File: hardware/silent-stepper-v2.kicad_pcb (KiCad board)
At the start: 4 copper layers, 80 x 80 mm, 89 parts, among them P1 VIN, P101 CON-SENSOR2, P102 DEBUG, P103 BOOT, P2 OUT, P3 GPIO, P4 PROTO, Q1 CSD19533Q5A, Q2 CSD19533Q5A, Q3 CSD19533Q5A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

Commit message: finished prototype ready for revision
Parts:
- removed R101: 1k, kicad-libraries:R0603F
- added C30: 100nF, kicad-libraries:C0603F, F.Cu at (58.5, 98.8)
- added D3: red, kicad-libraries:D0603E, F.Cu at (98.7, 93.0)
- added D4: blue, kicad-libraries:D0603E, F.Cu at (112.8, 93.0)
- added D5: blue, kicad-libraries:D0603E, F.Cu at (117.5, 93.0)
- added D6: blue, kicad-libraries:D0603E, F.Cu at (108.1, 93.0)
- added D7: blue, kicad-libraries:D0603E, F.Cu at (103.4, 93.0)
- added G***: LOGO, kicad-libraries:Logo_CoMCU, B.Cu at (85.0, 101.9)
- added G***: LOGO, kicad-libraries:Logo_TF_10x12, F.Cu at (51.0, 104.8)
- added R25: 1k, kicad-libraries:R0603F, F.Cu at (108.4, 98.5)
- added R26: 1k, kicad-libraries:R0603F, F.Cu at (103.2, 98.5)
- added RP4: 1k, kicad-libraries:0603X4, F.Cu at (105.8, 98.5)
- added U4: DRILL, kicad-libraries:DRILL_NP, F.Cu at (47.5, 142.5)
- added U5: DRILL, kicad-libraries:DRILL_NP, F.Cu at (47.5, 117.5)
- added U6: DRILL, kicad-libraries:DRILL_NP, F.Cu at (122.5, 117.5)
- added U7: DRILL, kicad-libraries:DRILL_NP, F.Cu at (122.5, 142.5)
- added VAL: CE_5mm, kicad-libraries:CE_5mm, B.Cu at (93.0, 101.9)
- added VAL: WEEE_7mm, kicad-libraries:WEEE_7mm, B.Cu at (77.8, 102.4)
- C3: value 100nF -> 220nF
- RP2: footprint kicad-libraries:0603X4 -> kicad-libraries:4X0402
- moved D101 71.1 mm to (94.0, 93.0), turned to 270 degrees
- moved C102 63.5 mm to (88.6, 97.4), turned to 90 degrees
- moved RP101 60.2 mm to (86.9, 97.4)
- moved C2 46.5 mm to (69.3, 103.1), turned to 270 degrees
- moved X1 43.8 mm to (71.7, 99.7), turned to 90 degrees
- moved C1 42.4 mm to (71.7, 102.0), turned to 180 degrees
- moved C4 39.6 mm to (71.7, 97.4)
- moved P102 38.1 mm to (65.3, 92.0)
- moved P103 34.5 mm to (63.5, 91.9), turned to 270 degrees
- moved C104 33.7 mm to (61.5, 104.2), turned to 180 degrees
- moved RP1 30.8 mm to (64.7, 110.2), turned to 180 degrees
- moved C3 21.3 mm to (57.0, 98.8), turned to 90 degrees
- moved P4 20.1 mm to (123.6, 102.2), turned to 90 degrees
- moved R23 15.2 mm to (53.9, 149.9)
- moved P3 15.2 mm to (47.8, 155.2)
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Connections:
- RP1 pad 5: DIAG1 -> Net-(RP1-Pad5)
- RP1 pad 6: DIAG0 -> Net-(RP1-Pad6)
- RP1 pad 8: DRV_ENN -> Net-(RP1-Pad8)
- RP101 pad 1: Net-(P101-Pad4) -> S-CS
- RP101 pad 2: Net-(P101-Pad5) -> S-CLK
- RP101 pad 3: Net-(P101-Pad6) -> S-MOSI
- RP101 pad 4: Net-(C102-Pad2) -> S-MISO
- RP101 pad 5: S-MISO -> Net-(C102-Pad2)
- RP101 pad 6: S-MOSI -> Net-(P101-Pad6)
- RP101 pad 7: S-CLK -> Net-(P101-Pad5)
- RP101 pad 8: S-CS -> Net-(P101-Pad4)
- RP3 pad 5: Net-(RP3-Pad5) -> Net-(RP1-Pad8)
- RP3 pad 7: Net-(RP3-Pad7) -> Net-(RP1-Pad6)
- RP3 pad 8: Net-(RP3-Pad8) -> Net-(RP1-Pad5)
- U1 pad 23: Net-(P4-Pad2) -> Net-(P4-Pad3)
- U1 pad 24: Net-(P4-Pad3) -> Net-(P4-Pad2)
- U1 pad 26: Net-(RP3-Pad7) -> Net-(RP1-Pad6)
- U1 pad 27: Net-(RP3-Pad8) -> Net-(RP1-Pad5)
- U1 pad 28: Net-(RP3-Pad5) -> Net-(RP1-Pad8)
- U2 pad 11: Net-(U2-Pad11) -> GPIO0
- U2 pad 12: Net-(U2-Pad12) -> GPIO1
- U2 pad 13: Net-(P102-Pad1) -> Net-(U2-Pad13)
- U2 pad 4: GPIO0 -> Net-(P102-Pad1)
- U2 pad 5: GPIO1 -> Net-(U2-Pad5)
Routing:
- net VCC: track 0.00 -> 151.2 mm, vias 0 -> 4
- net Net-(R25-Pad2): track 0.00 -> 60.2 mm, vias 0 -> 2
- net Net-(RP4-Pad8): track 0.00 -> 58.7 mm, vias 0 -> 2
- net GND: track 8.45 -> 66.4 mm, vias 52 -> 142
- net Net-(RP4-Pad7): track 0.00 -> 56.1 mm, vias 0 -> 2
- net Net-(RP4-Pad6): track 0.00 -> 55.2 mm, vias 0 -> 2
- net Net-(RP4-Pad5): track 0.00 -> 54.9 mm, vias 0 -> 2
- net Net-(R26-Pad2): track 0.00 -> 49.8 mm, vias 0 -> 2
- net GPIO0: track 0.00 -> 41.8 mm
- net GPIO1: track 0.00 -> 41.6 mm
- net Net-(P4-Pad1): track 0.00 -> 39.0 mm, vias 0 -> 1
- net Net-(P4-Pad2): track 0.00 -> 37.1 mm, vias 0 -> 1
- net Net-(P4-Pad3): track 0.00 -> 36.0 mm, vias 0 -> 1
- net Net-(P4-Pad4): track 0.00 -> 33.5 mm, vias 0 -> 1
- net Net-(P4-Pad5): track 0.00 -> 33.5 mm, vias 0 -> 1
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- added copper zone on In2.Cu, net GND
- added copper zone on In1.Cu, net Net-(C13-Pad1)
- added copper zone on In2.Cu, net Net-(C13-Pad1)
- added copper zone on In1.Cu, net Net-(C14-Pad1)
- added copper zone on In2.Cu, net Net-(C14-Pad1)
- added copper zone on In1.Cu, net Net-(C15-Pad1)
- added copper zone on In2.Cu, net Net-(C15-Pad1)
- added copper zone on In1.Cu, net Net-(C16-Pad1)
- added copper zone on In2.Cu, net Net-(C16-Pad1)
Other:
- rule pad_to_mask_clearance: 0.051 -> 0
- board text added: "+"
- board text added: "-"
- board text added: "ENCA"
- board text added: "ENCB"
- board text added: "ENCN"
- board text added: "Enable"
- board text added: "Error"
- board text added: "GPIO0"
- board text added: "GPIO1"
- board text added: "Input 10-48V"
- board text added: "MA1"
- board text added: "MA2"
- board text added: "MB1"
- board text added: "MB2"
- board text added: "REFL"
- board text added: "REFR"
- board text added: "Silent Stepper 2.0"
- board text added: "Status"
- board text added: "Steps"

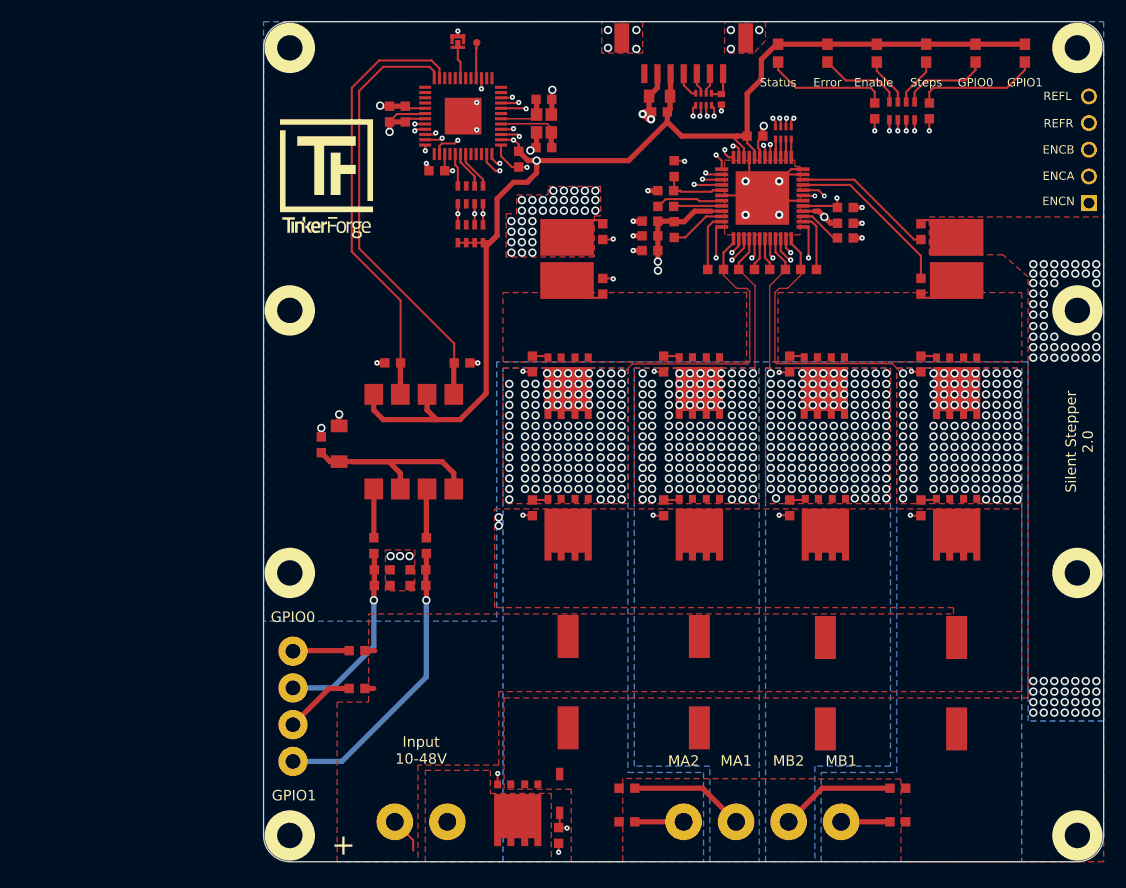
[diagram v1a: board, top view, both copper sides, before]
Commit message: changes protection circuit
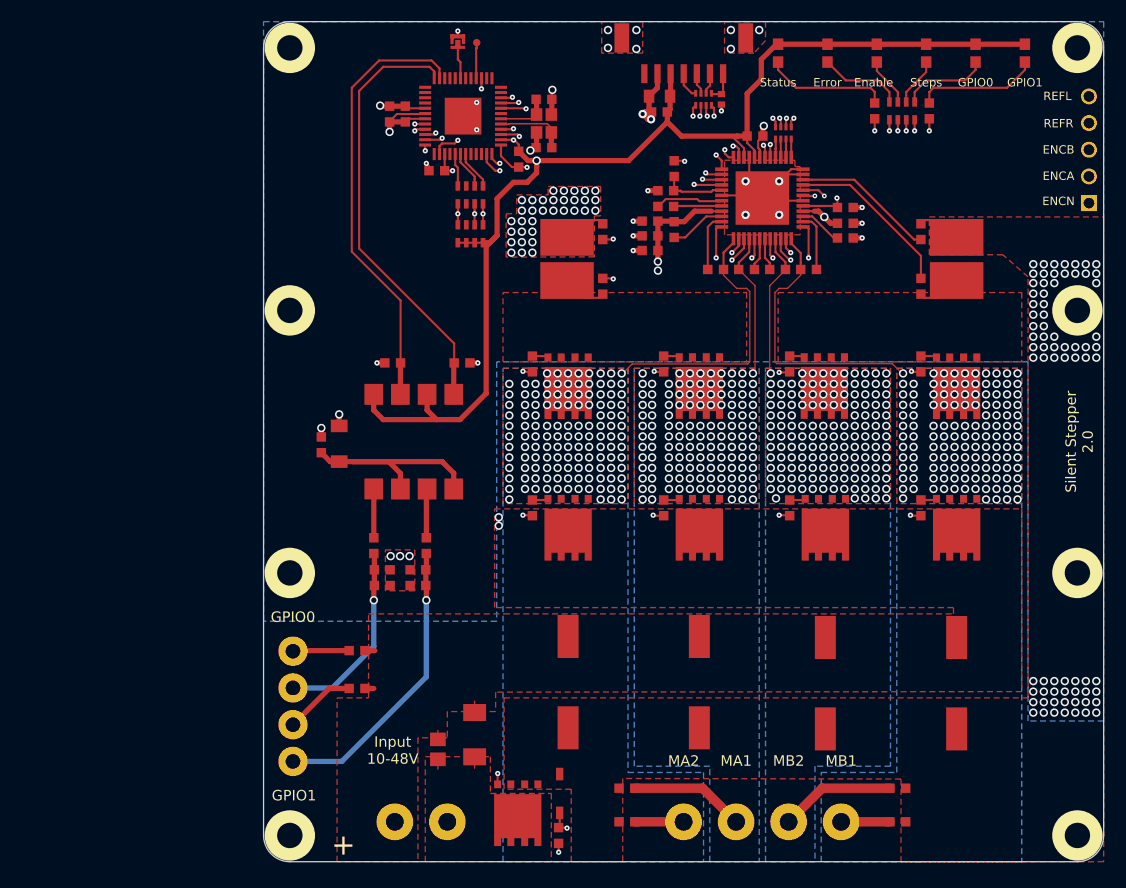
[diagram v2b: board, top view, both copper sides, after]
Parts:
- removed G***: LOGO, kicad-libraries:Logo_CoMCU
- removed G***: LOGO, kicad-libraries:Logo_TF_10x12
- removed VAL: CE_5mm, kicad-libraries:CE_5mm
- removed VAL: WEEE_7mm, kicad-libraries:WEEE_7mm
- added D8: SMBJ24CA, kicad-libraries:SMB, F.Cu at (65.1, 157.9)
- added PTC1: VC080526C580DP, kicad-libraries:R0805E, F.Cu at (61.6, 159.3)
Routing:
- net Net-(D8-Pad2): track 0.00 -> 2.04 mm
- net V_GPIO: track 91.9 -> 90.4 mm
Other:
- board text added: "IN"

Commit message: ready for prototype
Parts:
- added Fiducial_Mark: VAL**, kicad-libraries:Fiducial_Mark, F.Cu at (101.0, 114.0)
- added Fiducial_Mark: VAL**, kicad-libraries:Fiducial_Mark, F.Cu at (64.0, 143.0)
- added Fiducial_Mark: VAL**, kicad-libraries:Fiducial_Mark, F.Cu at (116.0, 99.0)
- added Fiducial_Mark: VAL**, kicad-libraries:Fiducial_Mark, F.Cu at (53.0, 94.0)
- added G***: LOGO, kicad-libraries:TF_LOGO_70MM, B.Cu at (85.0, 103.5)
- added G***: LOGO, kicad-libraries:Logo_CoMCU, B.Cu at (85.0, 153.0)
- added G***: LOGO, kicad-libraries:Logo_TF_10x12, F.Cu at (52.0, 108.5)
- added VAL: WEEE_7mm, kicad-libraries:WEEE_7mm, B.Cu at (76.9, 153.4)
- added VAL: CE_5mm, kicad-libraries:CE_5mm, B.Cu at (93.0, 153.0)

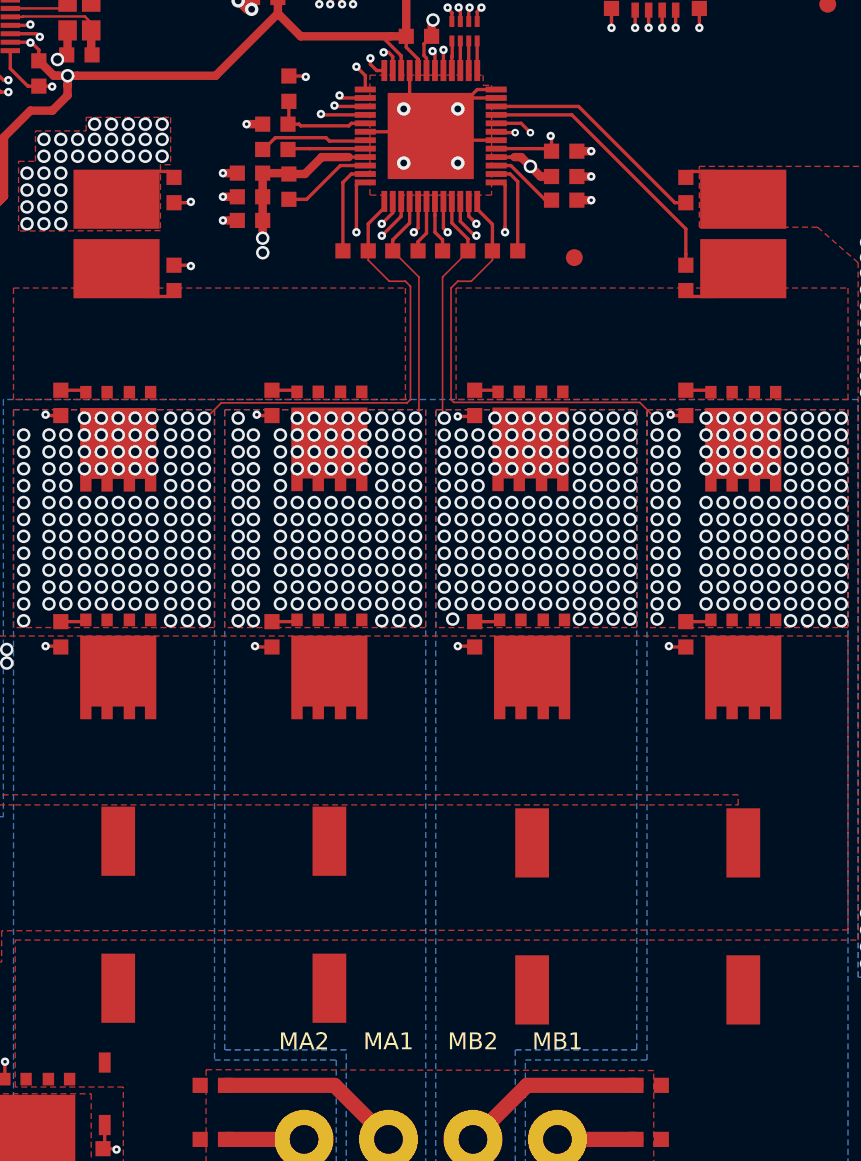
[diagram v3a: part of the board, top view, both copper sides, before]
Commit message: DRC control and ordered prototyp
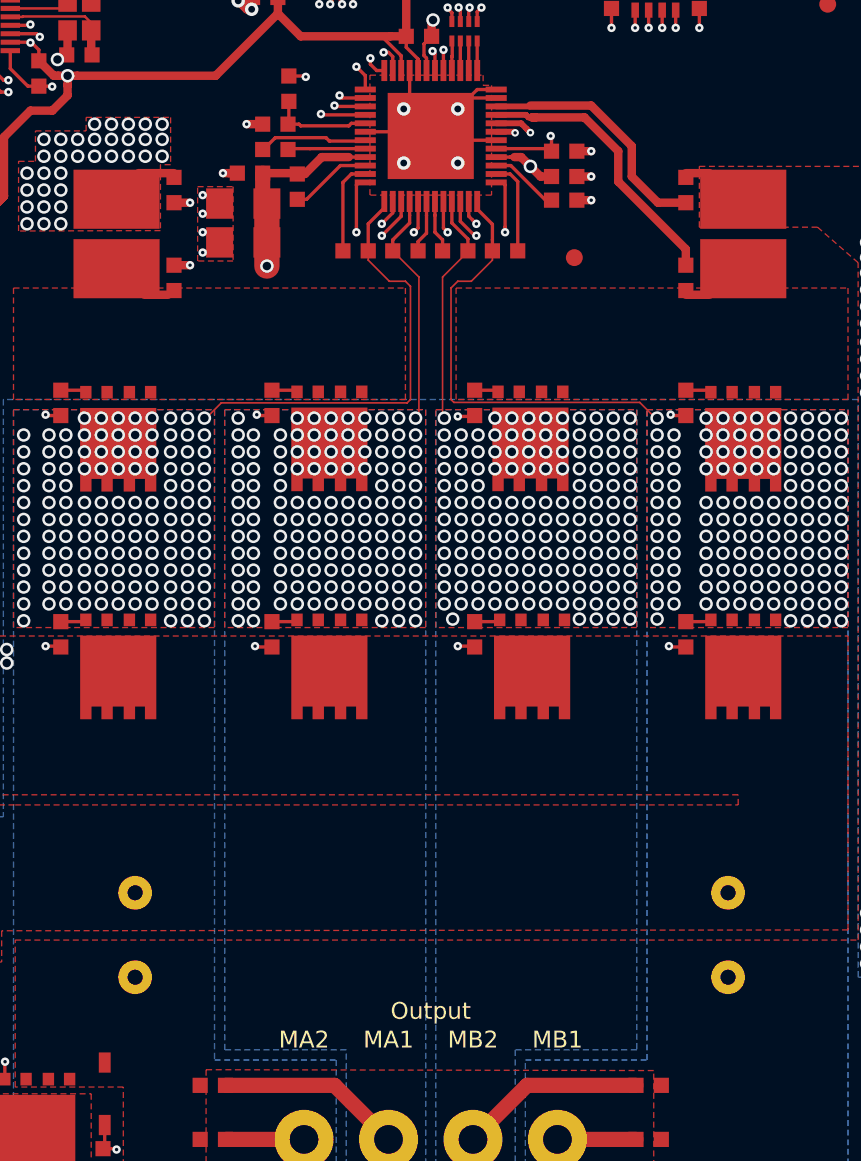
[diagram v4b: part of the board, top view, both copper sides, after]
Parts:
- removed C19, C22: 220uF/100V/LowESR, kicad-libraries:ELKO_103
- C17, C18: footprint kicad-libraries:C0603F -> kicad-libraries:C1206E
- C20, C21: value 220uF/100V/LowESR -> 220uF/100V/UVY2A221MHD1TO; footprint kicad-libraries:ELKO_103 -> kicad-libraries:ELKO_RAD_12
- moved C21 36.1 mm to (110.1, 154.1)
- moved C20 23.5 mm to (75.0, 154.1)
- moved VAL 8.39 mm to (85.2, 154.6)
- moved G*** 7.60 mm to (92.5, 154.2)
- moved VAL 7.58 mm to (100.5, 154.1)
- moved C18 1.36 mm to (81.4, 113.1)
- moved C17 0.57 mm to (81.4, 110.8)
- moved C11 0.50 mm to (84.6, 109.8)
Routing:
- net Net-(R7-Pad2): track 13.6 -> 14.7 mm
- net V_GPIO: track 90.4 -> 89.8 mm, vias 6 -> 5
- net Net-(R6-Pad2): track 16.2 -> 16.7 mm
- net Net-(C11-Pad2): track 5.35 -> 4.85 mm
- net GND: track 66.4 -> 66.7 mm, vias 142 -> 144
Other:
- board text added: "Output"

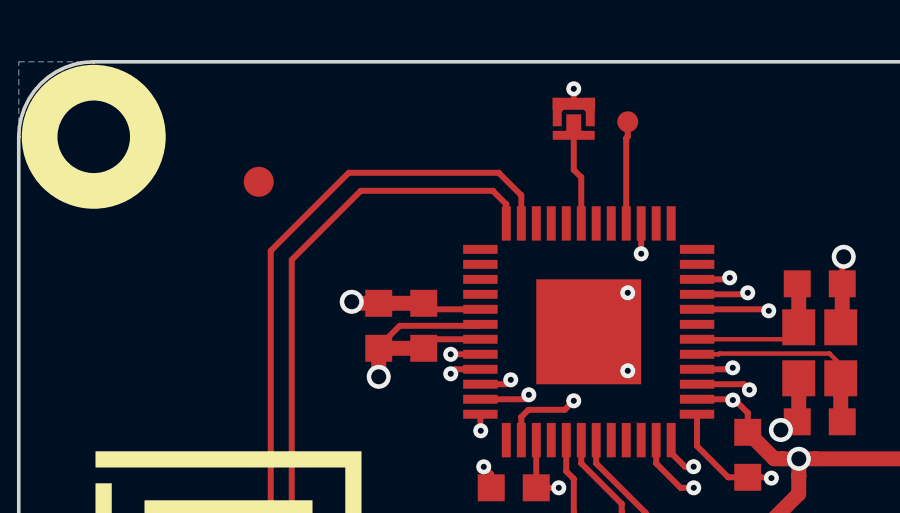
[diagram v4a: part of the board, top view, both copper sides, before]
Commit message: changed GPIO interrupt pin and added zener value
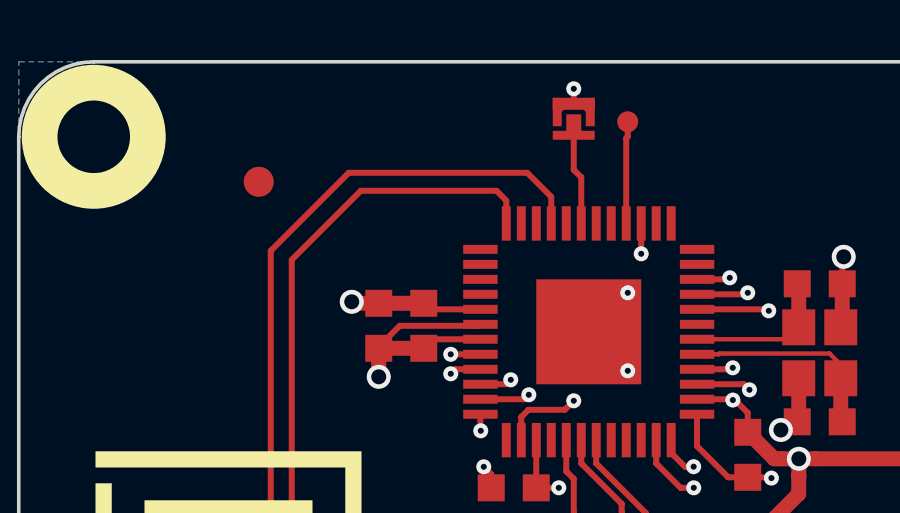
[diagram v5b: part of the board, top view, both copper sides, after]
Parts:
- D2: value TBD! -> Z3,3V
- P1: footprint kicad-libraries:OQ_2P_5mm_Vertical -> kicad-libraries:OQ_2P_5mm_Vertical_Black
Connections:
- U2 pad 11: GPIO0 -> Net-(U2-Pad11)
- U2 pad 9: Net-(U2-Pad9) -> GPIO0
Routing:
- net GPIO0: track 41.8 -> 42.8 mm

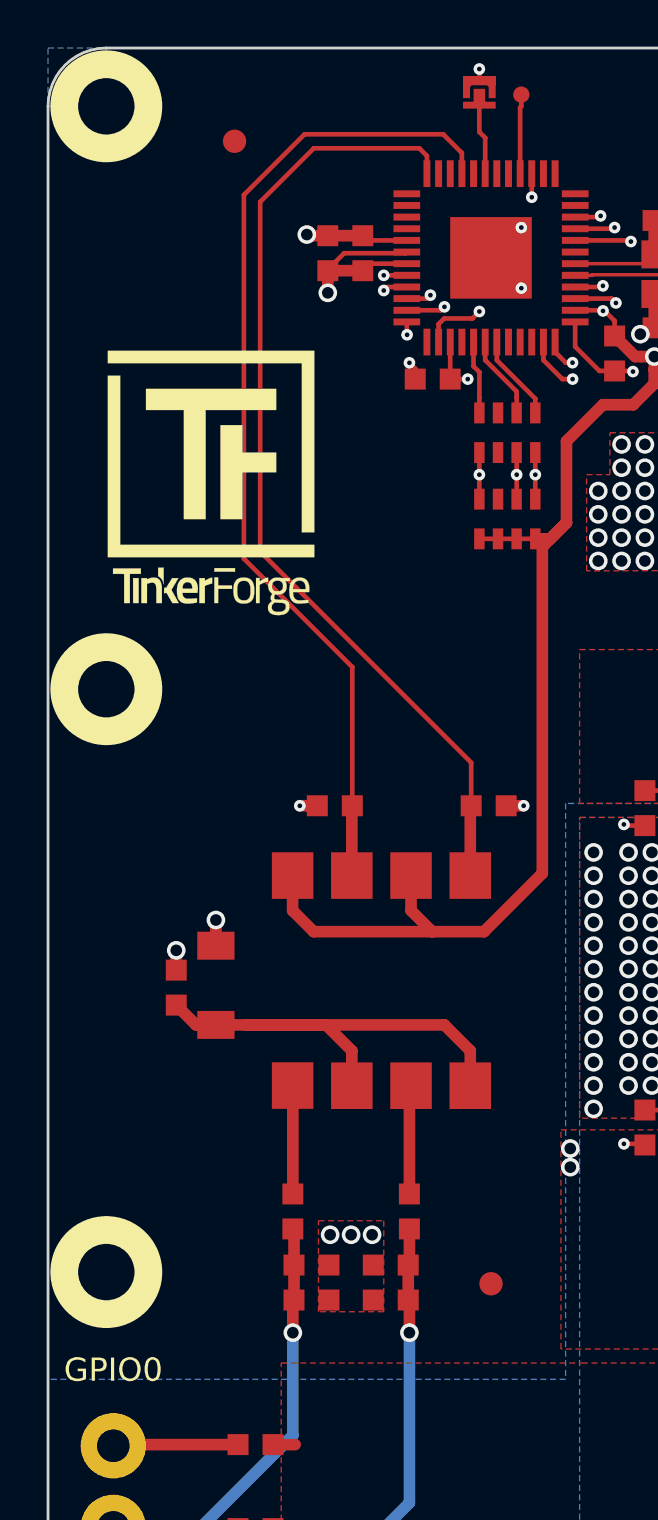
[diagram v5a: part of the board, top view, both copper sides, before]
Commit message: added Voltage In Sense
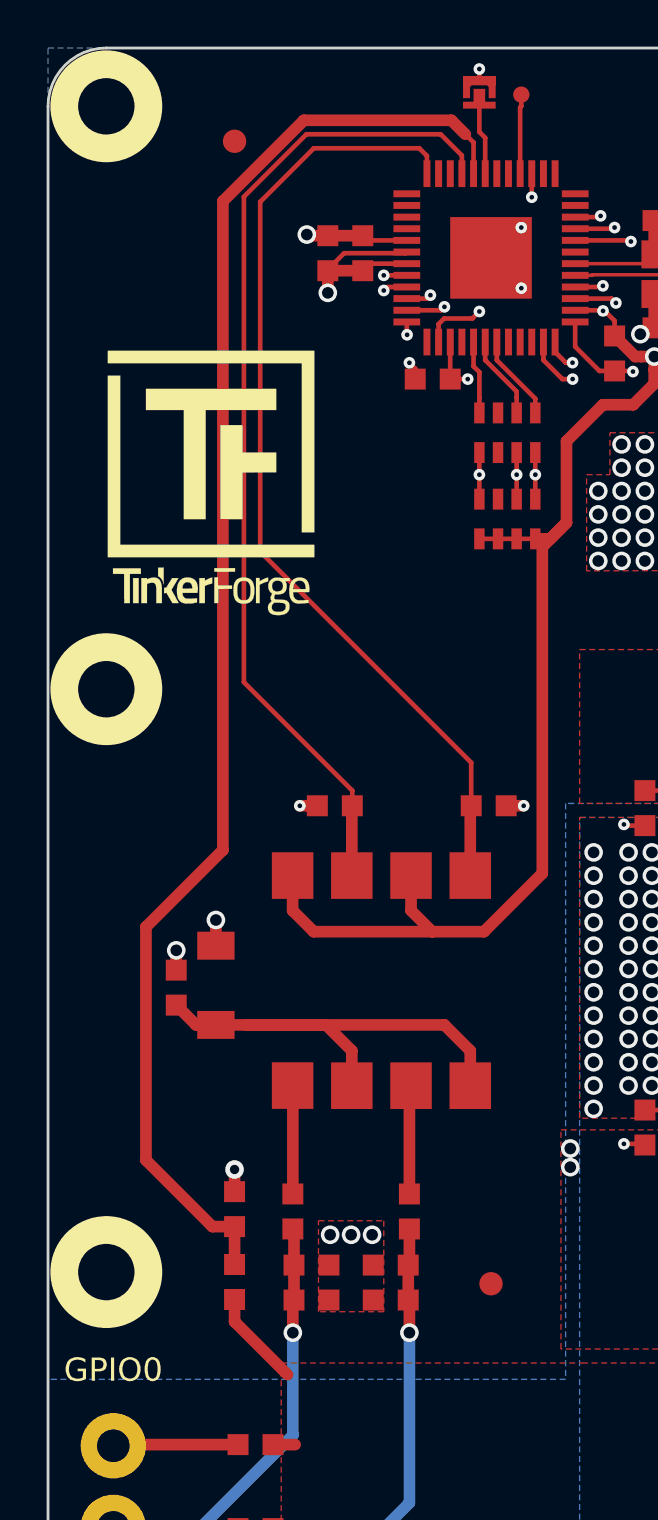
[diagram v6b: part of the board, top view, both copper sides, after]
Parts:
- added R27: 10k, kicad-libraries:R0603F, F.Cu at (53.0, 139.8)
- added R28: 150k, kicad-libraries:R0603F, F.Cu at (53.0, 142.9)
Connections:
- U2 pad 8: Net-(U2-Pad8) -> V_Sense
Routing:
- net V_Sense: track 0.00 -> 63.0 mm
- net V_GPIO: track 89.8 -> 94.0 mm
- net GND: track 66.7 -> 67.7 mm, vias 144 -> 145
